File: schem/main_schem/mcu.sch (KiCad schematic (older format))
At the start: 31 parts, among them P1 CONN_ICD, SW1 SW_RESET, U1 25LC256, U2 PIC18F97J60, X1 25MHz

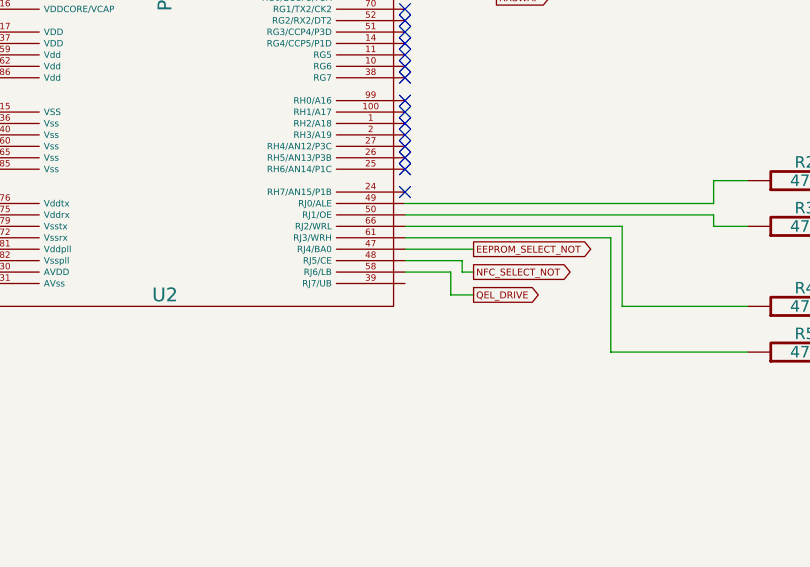
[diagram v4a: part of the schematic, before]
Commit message: linear regulators for logic/mcu
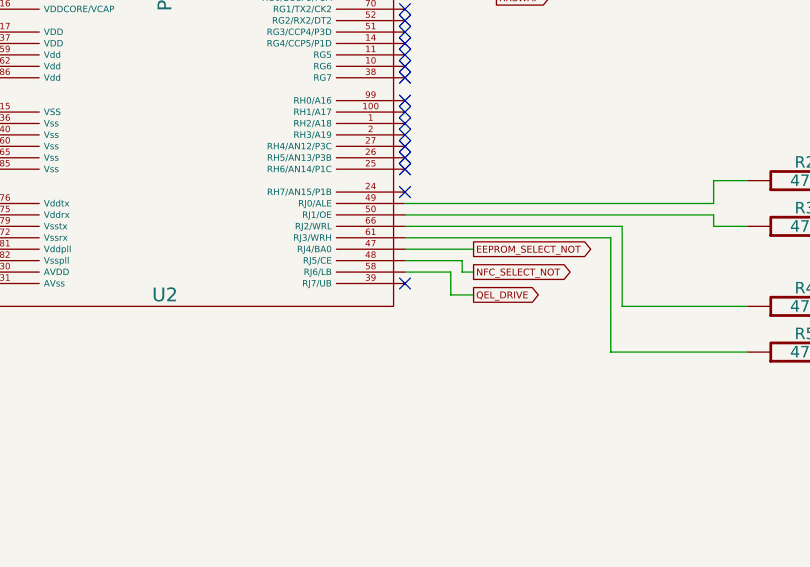
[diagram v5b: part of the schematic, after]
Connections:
- no-connect marks 50 -> 51
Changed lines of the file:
@@
-EESchema Schematic File Version 2  date 9/29/2012 1:33:09 PM
+EESchema Schematic File Version 2  date 9/29/2012 2:30:36 PM
 LIBS:power
 LIBS:device
@@
 Comment4 ""
 $EndDescr
+NoConn ~ 7100 5250
 NoConn ~ 5200 2450
 NoConn ~ 5200 2400
